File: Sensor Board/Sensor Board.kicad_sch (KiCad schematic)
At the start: 21 parts, among them J1 Programming Header, J3 Micro_SD_Card, U1 PIC18F26K83, U3 MCP2562, Y1 12MHz Crystal

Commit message: fixed footprints not loading
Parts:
- J1: footprint Canhw:PinSocket_5x2.54_SMD_90deg_952-3198-1-ND -> canhw:PinSocket_5x2.54_SMD_90deg_952-3198-1-ND
- J3: footprint Canhw:microSD_Molex_WM6698CT-ND -> canhw:microSD_Molex_WM6698CT-ND
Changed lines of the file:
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@@
 			)
 		)
-		(property "Footprint" "Canhw:microSD_Molex_WM6698CT-ND"
+		(property "Footprint" "canhw:microSD_Molex_WM6698CT-ND"
 			(at 148.59 152.4 0)
 			(effects
@@
 			)
 		)
-		(property "Footprint" "Canhw:PinSocket_5x2.54_SMD_90deg_952-3198-1-ND"
+		(property "Footprint" "canhw:PinSocket_5x2.54_SMD_90deg_952-3198-1-ND"
 			(at 210.82 34.29 0)
 			(effects

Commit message: did layout
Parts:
- removed R2: 10kR, Resistor_SMD:R_0805_2012Metric_Pad1.20x1.40mm_HandSolder, symbol Device:R_US
- added R14: 10kR, Resistor_SMD:R_0805_2012Metric_Pad1.20x1.40mm_HandSolder, symbol Device:R_US
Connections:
- net +3V3D: now also R14.1
- net CANRX: now also U1.11 (RC0); no longer U1.25 (RB4)
- net CANTX: now also U1.12 (RC1); no longer U1.26 (RB5)
- net CURR_SENSE: now also U1.26 (RB5); no longer U1.4 (RA2)
- net MISO: now also J3.7 (DAT0), R3.2, U1.15 (RC4); no longer U1.16 (RC5)
- net MOSI: now also J3.3 (CMD), R4.2, U1.16 (RC5); no longer U1.15 (RC4)
- net SCLK: now also J3.5 (CLK)
- net at R10.2: now also U1.4 (RA2); no longer U1.17 (RC6)
- net at J3.1 (DAT2): no longer R4.2
- net CS renamed CS_ADC
- net IRR_SENSE: no longer names the net of U1.18 (RC7)
- net PIC_MICRO_SD_CS: no longer names the net of U1.21 (RB0)
- net PIC_MICRO_SD_CS: no longer J3.2 (DAT3/CD)
- net PIC_MICRO_SD_SCK: no longer names the net of U1.23 (RB2)
- net PIC_MICRO_SD_SCK: no longer J3.5 (CLK)
- removed net PIC_MICRO_SD_SDI: J3.7 (DAT0), R3.2, U1.24 (RB3)
- net PIC_MICRO_SD_SDO: no longer names the net of U1.22 (RB1)
- net PIC_MICRO_SD_SDO: no longer J3.3 (CMD)
- new net CS_SD: J3.2 (DAT3/CD), R14.2, U1.17 (RC6)
- no-connect marks 3 -> 9
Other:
- moved on the sheet: C4, D4, R10, R3, R8, U1

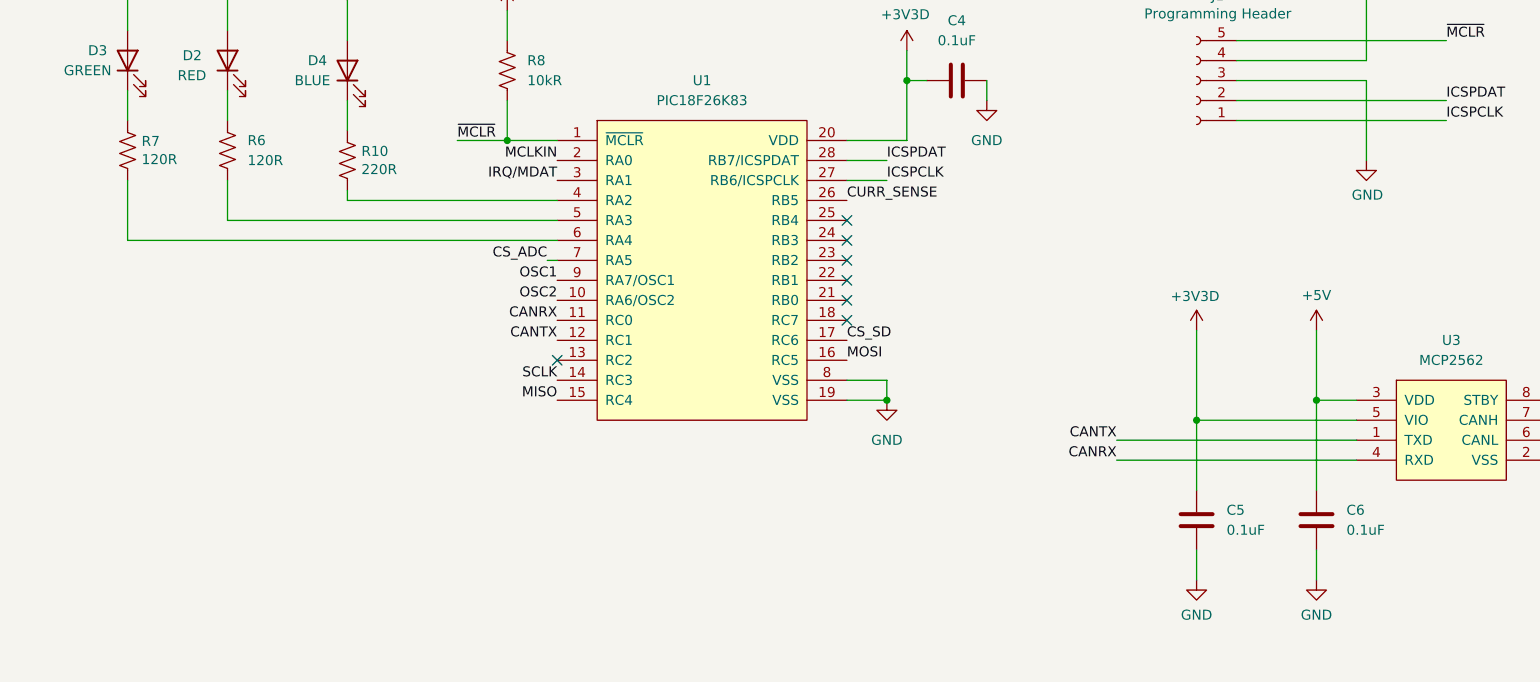
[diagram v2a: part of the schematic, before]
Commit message: implemented Joe's comments
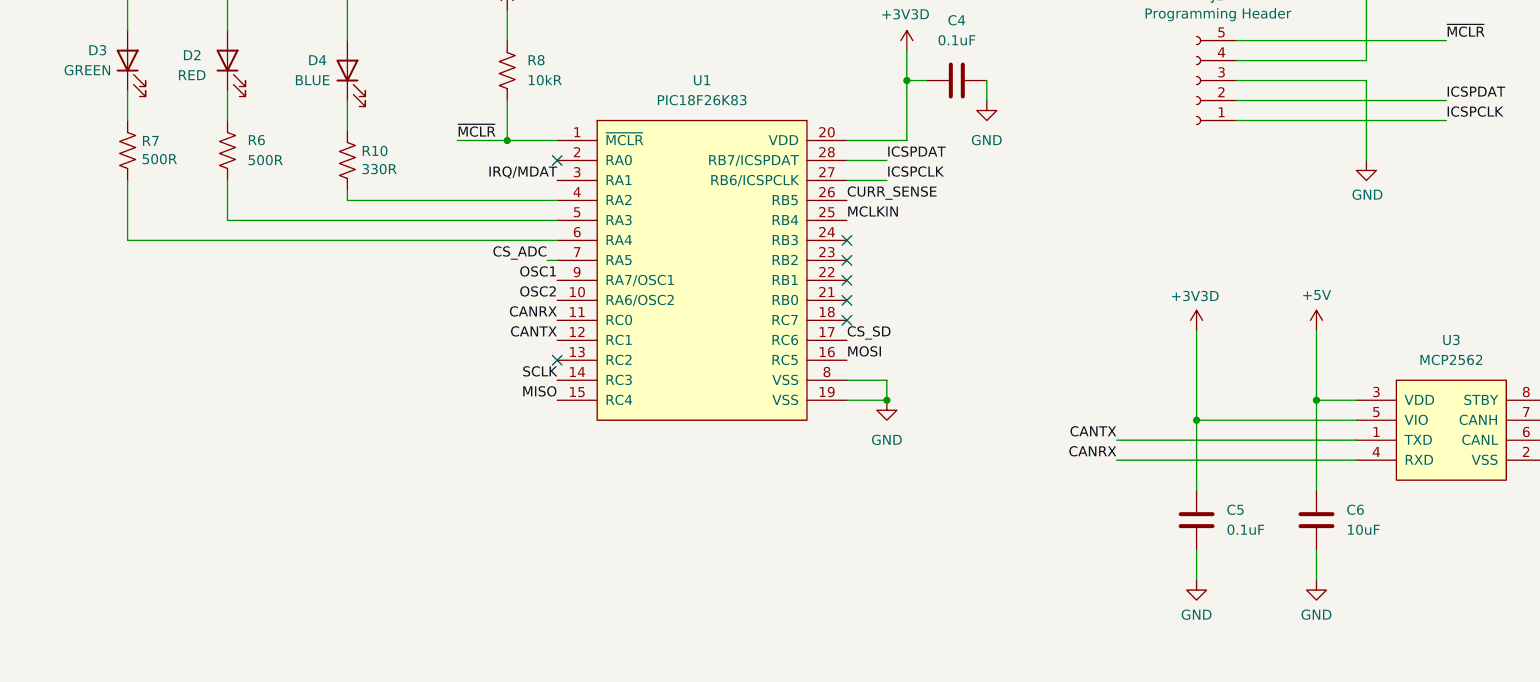
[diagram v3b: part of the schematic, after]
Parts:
- C6: value 0.1uF -> 10uF
- R10: value 220R -> 330R
- R6, R7: value 120R -> 500R
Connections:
- net MCLKIN: now also U1.25 (RB4); no longer U1.2 (RA0)
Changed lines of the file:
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@@
 	)
 	(no_connect
-		(at 166.37 52.07)
-	)
-	(no_connect
 		(at 166.37 59.69)
 	)
@@
 	)
 	(no_connect
+		(at 129.54 44.45)
+	)
+	(no_connect
 		(at 166.37 64.77)
 	)
@@
 	)
 	(label "MCLKIN"
-		(at 129.54 44.45 180)
+		(at 166.37 52.07 0)
 		(effects
 			(font
 				(size 1.27 1.27)
 			)
-			(justify right bottom)
+			(justify left bottom)
 		)
 	)
@@
 			)
 		)
-		(property "Value" "220R"
+		(property "Value" "330R"
 			(at 104.648 45.593 0)
 			(effects
@@
 			)
 		)
-		(property "Value" "0.1uF"
+		(property "Value" "10uF"
 			(at 229.87 91.4399 0)
 			(effects
@@
 			)
 		)
-		(property "Value" "120R"
+		(property "Value" "500R"
 			(at 90.17 44.4499 0)
 			(effects
@@
 			)
 		)
-		(property "Value" "120R"
+		(property "Value" "500R"
 			(at 76.708 44.323 0)
 			(effects
